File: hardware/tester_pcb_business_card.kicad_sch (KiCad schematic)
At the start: 46 parts, among them J1 SWIO, SW1 PWR, SW2 A, SW3 B, SW4 C, SW5 D, SW6 RST, U1 CH32V003FxUx

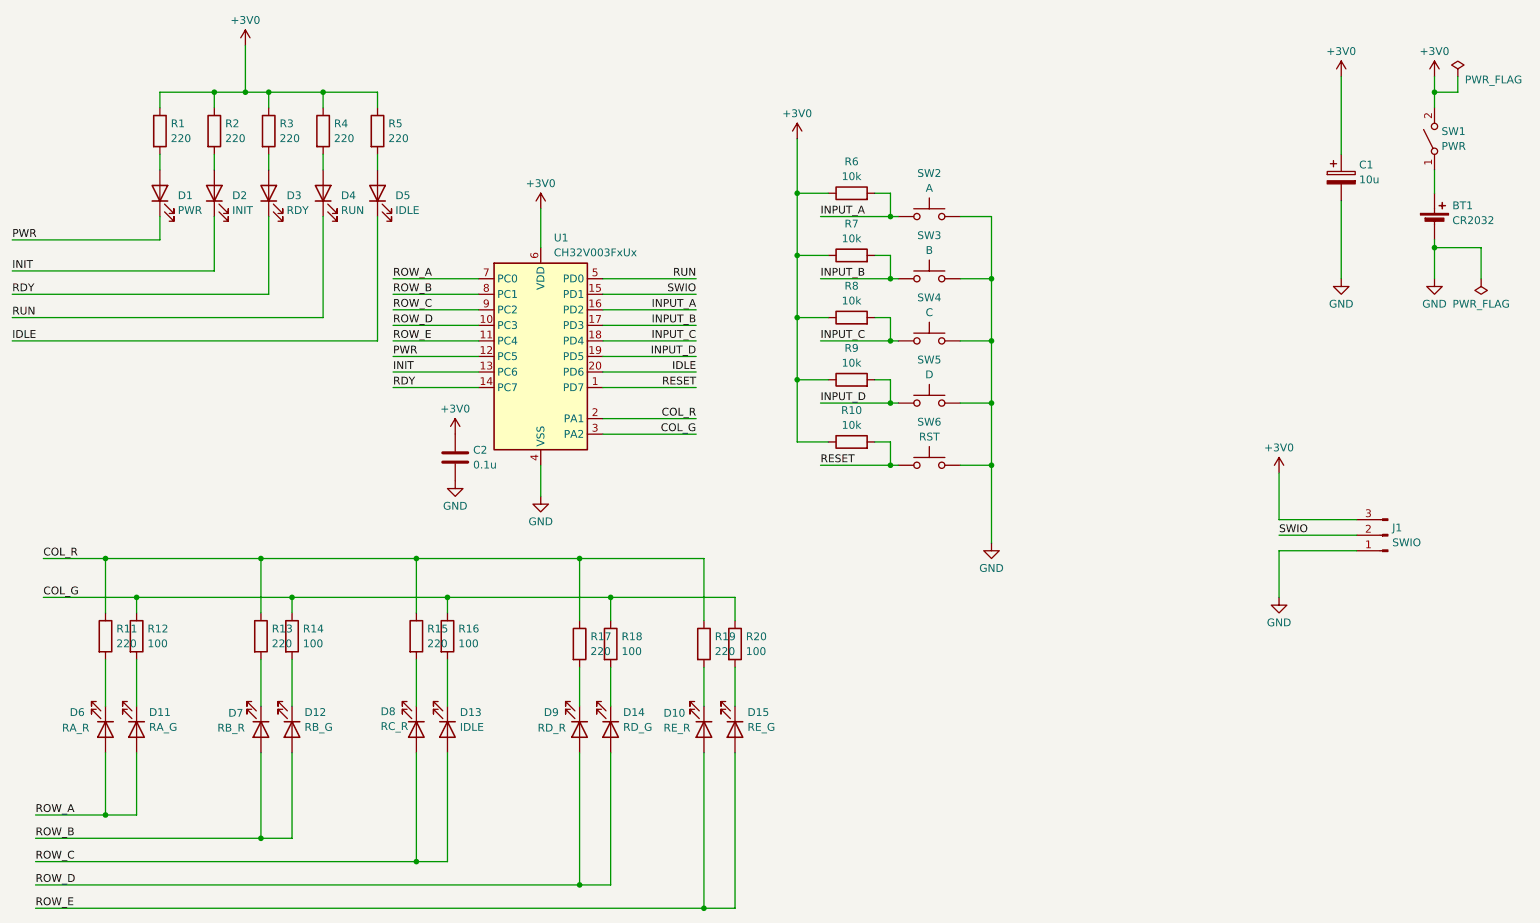
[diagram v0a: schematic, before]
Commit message: Update LED resistor values after tuning
LEDs were way too bright with chosen resistor values. Tuned so all LEDs are of a similar brightness and to reduce current draw.
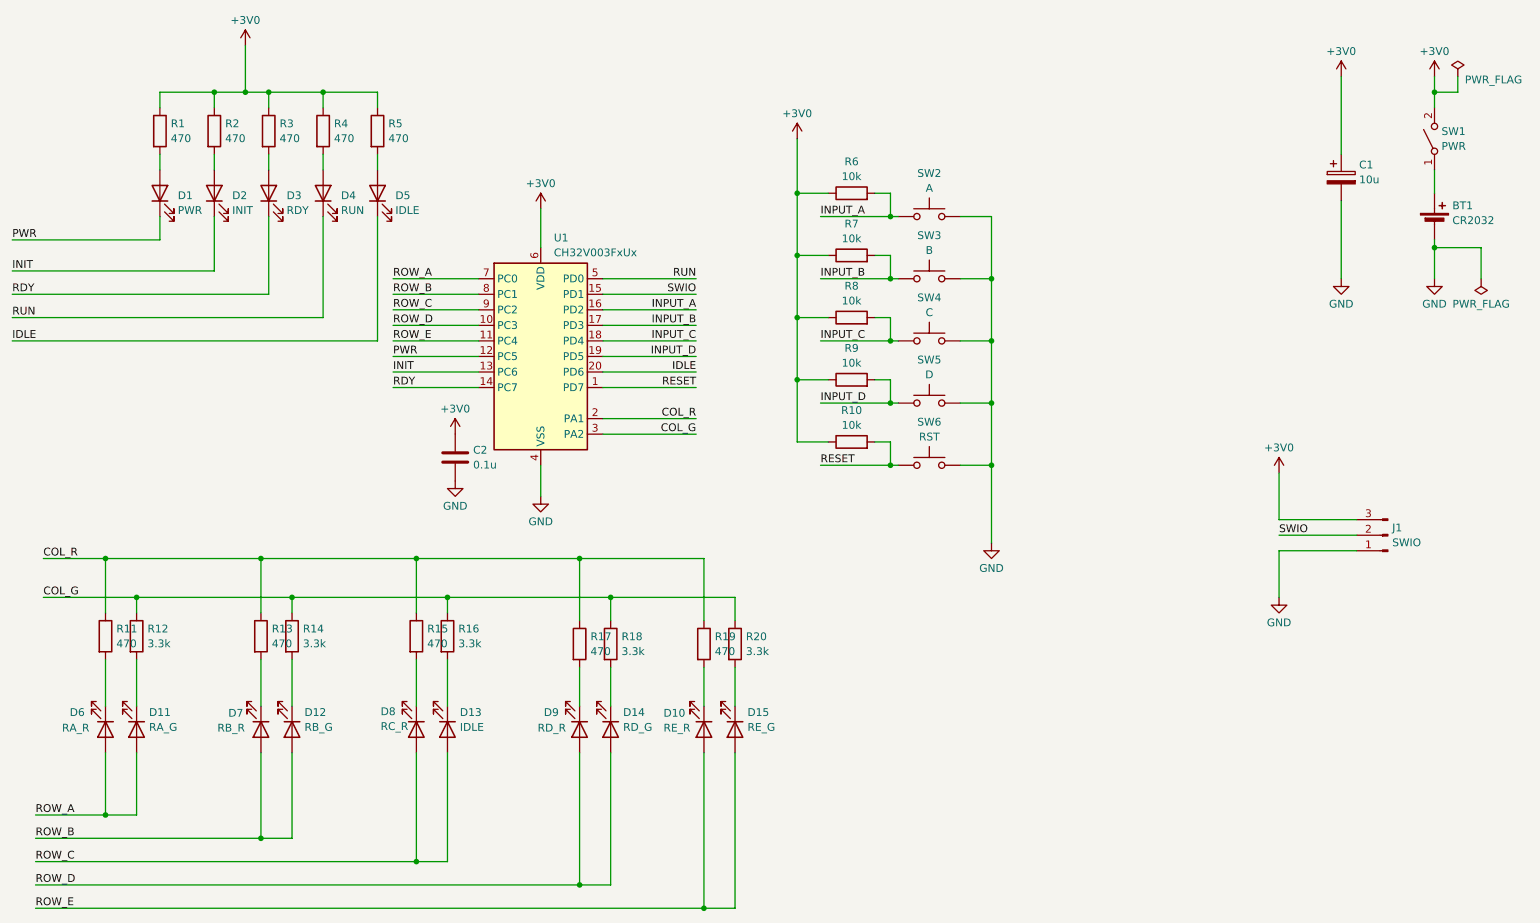
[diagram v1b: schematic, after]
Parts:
- R1, R11, R13, R15, R17, R19, R2, R3, R4, R5: value 220 -> 470; LCSC C22962 -> C23179
- R12, R14, R16, R18, R20: value 100 -> 3.3k; LCSC C17408 -> C22978
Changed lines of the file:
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@@
 			)
 		)
-		(property "Value" "100"
+		(property "Value" "3.3k"
 			(at 95.758 124.4021 0)
 			(effects
@@
 			)
 		)
-		(property "LCSC" "C17408"
+		(property "LCSC" "C22978"
 			(at 93.98 123.19 0)
 			(effects
@@
 			)
 		)
-		(property "Value" "100"
+		(property "Value" "3.3k"
 			(at 122.428 125.6721 0)
 			(effects
@@
 			)
 		)
-		(property "LCSC" "C17408"
+		(property "LCSC" "C22978"
 			(at 120.65 124.46 0)
 			(effects
@@
 			)
 		)
-		(property "Value" "220"
+		(property "Value" "470"
 			(at 48.768 41.8521 0)
 			(effects
@@
 			)
 		)
-		(property "LCSC" "C22962"
+		(property "LCSC" "C23179"
 			(at 46.99 40.64 0)
 			(effects
@@
 			)
 		)
-		(property "Value" "220"
+		(property "Value" "470"
 			(at 137.668 125.6721 0)
 			(effects
@@
 			)
 		)
-		(property "LCSC" "C22962"
+		(property "LCSC" "C23179"
 			(at 135.89 124.46 0)
 			(effects
@@
 			)
 		)
-		(property "Value" "220"
+		(property "Value" "470"
 			(at 39.878 124.4021 0)
 			(effects
@@
 			)
 		)
-		(property "LCSC" "C22962"
+		(property "LCSC" "C23179"
 			(at 38.1 123.19 0)
 			(effects
@@
 			)
 		)
-		(property "Value" "220"
+		(property "Value" "470"
 			(at 66.548 41.8521 0)
 			(effects
@@
 			)
 		)
-		(property "LCSC" "C22962"
+		(property "LCSC" "C23179"
 			(at 64.77 40.64 0)
 			(effects
@@
 			)
 		)
-		(property "Value" "100"
+		(property "Value" "3.3k"
 			(at 70.358 124.4021 0)
 			(effects
@@
 			)
 		)
-		(property "LCSC" "C17408"
+		(property "LCSC" "C22978"
 			(at 68.58 123.19 0)
 			(effects
@@
 			)
 		)
-		(property "Value" "220"
+		(property "Value" "470"
 			(at 84.328 41.8521 0)
 			(effects
@@
 			)
 		)
-		(property "LCSC" "C22962"
+		(property "LCSC" "C23179"
 			(at 82.55 40.64 0)
 			(effects
@@
 			)
 		)
-		(property "Value" "220"
+		(property "Value" "470"
 			(at 117.348 125.6721 0)
 			(effects
@@
 			)
 		)
-		(property "LCSC" "C22962"
+		(property "LCSC" "C23179"
 			(at 115.57 124.46 0)
 			(effects
@@
 			)
 		)
-		(property "Value" "100"
+		(property "Value" "3.3k"
 			(at 142.748 125.6721 0)
 			(effects
@@
 			)
 		)
-		(property "LCSC" "C17408"
+		(property "LCSC" "C22978"
 			(at 140.97 124.46 0)
 			(effects
@@
 			)
 		)
-		(property "Value" "220"
+		(property "Value" "470"
 			(at 65.278 124.4021 0)
 			(effects
@@
 			)
 		)
-		(property "LCSC" "C22962"
+		(property "LCSC" "C23179"
 			(at 63.5 123.19 0)
 			(effects
@@
 			)
 		)
-		(property "Value" "100"
+		(property "Value" "3.3k"
 			(at 44.958 124.4021 0)
 			(effects
@@
 			)
 		)
-		(property "LCSC" "C17408"
+		(property "LCSC" "C22978"
 			(at 43.18 123.19 0)
 			(effects
@@
 			)
 		)
-		(property "Value" "220"
+		(property "Value" "470"
 			(at 90.678 124.4021 0)
 			(effects
@@
 			)
 		)
-		(property "LCSC" "C22962"
+		(property "LCSC" "C23179"
 			(at 88.9 123.19 0)
 			(effects
@@
 			)
 		)
-		(property "Value" "220"
+		(property "Value" "470"
 			(at 57.658 41.8521 0)
 			(effects
@@
 			)
 		)
-		(property "LCSC" "C22962"
+		(property "LCSC" "C23179"
 			(at 55.88 40.64 0)
 			(effects
@@
 			)
 		)
-		(property "Value" "220"
+		(property "Value" "470"
 			(at 75.438 41.8521 0)
 			(effects
@@
 			)
 		)
-		(property "LCSC" "C22962"
+		(property "LCSC" "C23179"
 			(at 73.66 40.64 0)
 			(effects

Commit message: Fix test case LEDs rows and cols
I had them labelled the wrong way round. Didn't affect anything but it was confusing when referring to schematic when writing code for the test case LEDs.
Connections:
- net COL_G renamed ROW_G
- net COL_R renamed ROW_R
- net ROW_A renamed COL_A
- net ROW_B renamed COL_B
- net ROW_C renamed COL_C
- net ROW_D renamed COL_D
- net ROW_E renamed COL_E
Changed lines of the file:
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@@
 		)
 	)
-	(label "ROW_E"
+	(label "COL_E"
 		(at 26.67 167.64 0)
 		(effects
@@
 		)
 	)
-	(label "COL_G"
+	(label "ROW_G"
 		(at 134.62 90.17 180)
 		(effects
@@
 		)
 	)
-	(label "ROW_C"
+	(label "COL_C"
 		(at 85.09 69.85 0)
 		(effects
@@
 		)
 	)
-	(label "COL_R"
+	(label "ROW_R"
 		(at 27.94 110.49 0)
 		(effects
@@
 		)
 	)
-	(label "ROW_D"
+	(label "COL_D"
 		(at 26.67 163.83 0)
 		(effects
@@
 		)
 	)
-	(label "ROW_C"
+	(label "COL_C"
 		(at 26.67 160.02 0)
 		(effects
@@
 		)
 	)
-	(label "COL_R"
+	(label "ROW_R"
 		(at 134.62 87.63 180)
 		(effects
@@
 		)
 	)
-	(label "ROW_B"
+	(label "COL_B"
 		(at 85.09 67.31 0)
 		(effects
@@
 		)
 	)
-	(label "ROW_B"
+	(label "COL_B"
 		(at 26.67 156.21 0)
 		(effects
@@
 		)
 	)
-	(label "ROW_A"
+	(label "COL_A"
 		(at 85.09 64.77 0)
 		(effects
@@
 		)
 	)
-	(label "ROW_A"
+	(label "COL_A"
 		(at 26.67 152.4 0)
 		(effects
@@
 		)
 	)
-	(label "ROW_E"
+	(label "COL_E"
 		(at 85.09 74.93 0)
 		(effects
@@
 		)
 	)
-	(label "ROW_D"
+	(label "COL_D"
 		(at 85.09 72.39 0)
 		(effects
@@
 		)
 	)
-	(label "COL_G"
+	(label "ROW_G"
 		(at 27.94 116.84 0)
 		(effects

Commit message: PCBs for Ministry of Testing TestBash Brighton 2025
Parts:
- D13: value IDLE -> RC_G
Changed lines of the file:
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@@
 			)
 		)
-		(property "Value" "IDLE"
+		(property "Value" "RC_G"
 			(at 96.012 138.0546 90)
 			(effects
